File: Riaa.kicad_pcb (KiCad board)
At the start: 2 copper layers, 44 parts, among them J1 power, J2 in, J3 out, U1 TL071, U2 TL072, U3 TL071, U4 TL071

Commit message: layout
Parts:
- moved J2 136.9 mm to (17.8, 143.5)
- moved U4 131.1 mm to (127.0, 94.0), turned to 270 degrees
- moved R17 127.5 mm to (29.2, 123.2)
- moved R18 121.2 mm to (25.4, 132.1)
- moved R28 119.4 mm to (119.4, 121.9)
- moved R20 118.3 mm to (17.8, 125.7)
- moved R23 116.2 mm to (83.8, 128.3)
- moved R25 111.6 mm to (74.9, 120.7)
- moved R27 110.9 mm to (119.4, 108.0)
- moved R22 109.1 mm to (88.9, 116.8)
- moved U3 108.7 mm to (87.6, 95.2), turned to 270 degrees
- moved J3 108.1 mm to (110.5, 129.5)
- moved R24 108.0 mm to (85.1, 111.8)
- moved R15 108.0 mm to (22.9, 110.5)
- moved C9 105.5 mm to (132.1, 116.8)
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
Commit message: layout
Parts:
- moved R28 56.4 mm to (71.1, 92.7), turned to 270 degrees
- moved R23 54.9 mm to (53.3, 82.5), turned to 270 degrees
- moved J2 53.4 mm to (19.1, 90.2), turned to 90 degrees
- moved J1 52.6 mm to (67.3, 36.8)
- moved R27 48.6 mm to (78.7, 81.3), turned to 270 degrees
- moved C9 46.2 mm to (88.9, 100.3), turned to 90 degrees
- moved R22 45.9 mm to (58.4, 82.5), turned to 270 degrees
- moved J3 44.9 mm to (69.8, 110.5), turned to 90 degrees
- moved U4 44.5 mm to (82.5, 94.0)
- moved R16 37.7 mm to (35.6, 83.8), turned to 270 degrees
- moved C4 36.8 mm to (66.0, 48.3), turned to 90 degrees
- moved R24 32.1 mm to (58.4, 94.0), turned to 270 degrees
- moved U3 31.8 mm to (55.9, 94.0)
- moved R17 31.4 mm to (40.6, 94.0), turned to 270 degrees
- moved R18 29.6 mm to (40.6, 106.7), turned to 180 degrees
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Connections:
- R25 pad 1: Net-(R25-Pad1) -> GND
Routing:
- net Net-(C2-Pad1): track 0.00 -> 78.0 mm
- net Net-(C4-Pad1): track 0.00 -> 51.6 mm
- net Net-(J3-Pad1): track 0.00 -> 11.2 mm
- net Net-(R16-Pad2): track 0.00 -> 9.42 mm
- net Net-(C6-Pad1): track 0.00 -> 8.89 mm
- net GND: track 0.00 -> 7.44 mm
- net Net-(C5-Pad1): track 0.00 -> 6.35 mm
- net Net-(C6-Pad2): track 0.00 -> 5.08 mm

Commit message: decoupling
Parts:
- added C10: 100n, Capacitors_THT:C_Rect_L7.2mm_W2.5mm_P5.00mm_FKS2_FKP2_MKS2_MKP2, F.Cu at (67.3, 53.3)
- moved R9 33.2 mm to (77.5, 77.5), turned to 90 degrees
- moved C1 26.2 mm to (52.1, 64.8), turned to 270 degrees
- moved C4 25.5 mm to (68.6, 73.7), turned to 180 degrees
- moved R1 25.4 mm to (64.8, 50.8)
- moved R8 23.3 mm to (72.4, 66.0), turned to 180 degrees
- moved C2 18.2 mm to (58.4, 72.4), turned to 270 degrees
- moved R3 17.6 mm to (54.6, 50.8)
- moved R12 15.3 mm to (74.9, 68.6), turned to 90 degrees
- moved R10 11.4 mm to (85.1, 67.3), turned to 180 degrees
- moved R13 10.9 mm to (85.1, 59.7), turned to 180 degrees
- moved R7 10.9 mm to (62.2, 53.3), turned to 180 degrees
- moved R6 10.5 mm to (54.6, 55.9)
- moved R5 10.5 mm to (62.2, 66.0), turned to 90 degrees
- moved R4 9.92 mm to (59.7, 61.0), turned to 180 degrees
- moved J1 8.98 mm to (68.6, 45.7)
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
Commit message: routing
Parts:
- moved C7 24.3 mm to (49.5, 88.9)
- moved R20 20.4 mm to (43.2, 101.6)
- moved R21 19.1 mm to (45.7, 101.6)
- moved J2 15.9 mm to (33.0, 82.5)
- moved R16 10.8 mm to (43.2, 91.4), turned to 180 degrees
- moved R15 8.03 mm to (40.6, 86.4), turned to 180 degrees
- moved C5 6.84 mm to (35.6, 88.9), turned to 0 degrees
- moved C6 3.81 mm to (33.0, 106.7)
- moved R18 2.54 mm to (40.6, 104.1)
- moved R19 2.54 mm to (40.6, 106.7), turned to 0 degrees
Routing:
- net Net-(C6-Pad1): track 8.89 -> 30.0 mm
- net Net-(C7-Pad1): track 0.00 -> 11.2 mm
- net Net-(J3-Pad1): track 11.2 -> 18.8 mm
- net GND: track 7.44 -> 0.00 mm
- net Net-(C5-Pad1): track 6.35 -> 10.2 mm
- net Net-(C6-Pad2): track 5.08 -> 7.70 mm

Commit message: routing
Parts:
- moved J1 36.9 mm to (67.3, 82.5)
- moved R2 16.6 mm to (54.6, 71.1)
- moved C8 6.48 mm to (58.4, 90.2), turned to 0 degrees
- moved C2 4.02 mm to (59.7, 68.6)
- moved R10 3.81 mm to (85.1, 63.5)
- moved R13 2.84 mm to (82.5, 58.4)
- moved R22 2.84 mm to (55.9, 83.8)
- moved R11 2.54 mm to (77.5, 61.0)
- moved R4 2.54 mm to (59.7, 58.4)
- moved R28 1.80 mm to (69.8, 94.0)
- moved R14 1.27 mm to (74.9, 55.9)
- moved R23 1.27 mm to (53.3, 83.8)
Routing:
- net Net-(C9-Pad1): track 0.00 -> 23.7 mm
- net Net-(C10-Pad1): track 0.00 -> 14.5 mm
- net Net-(C2-Pad1): track 78.0 -> 91.5 mm
- net Net-(C1-Pad1): track 0.00 -> 9.42 mm
- net Net-(R22-Pad2): track 0.00 -> 8.67 mm
- net Net-(R10-Pad2): track 0.00 -> 6.13 mm
- net Net-(R11-Pad1): track 0.00 -> 6.13 mm
- net Net-(R4-Pad1): track 0.00 -> 6.13 mm
- net Net-(R12-Pad2): track 0.00 -> 5.08 mm
- net Net-(C10-Pad2): track 0.00 -> 5.08 mm
- net Net-(R5-Pad2): track 0.00 -> 5.08 mm
- net Net-(C4-Pad1): track 51.6 -> 55.2 mm
- net Net-(R6-Pad1): track 0.00 -> 2.54 mm
- net Net-(R13-Pad1): track 0.00 -> 2.54 mm
- net Net-(R1-Pad1): track 0.00 -> 2.54 mm
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
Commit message: layout
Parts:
- moved C2 24.1 mm to (67.3, 45.7), turned to 0 degrees
- moved C4 21.3 mm to (74.9, 53.3), turned to 0 degrees
- moved C3 16.6 mm to (82.5, 55.9), turned to 90 degrees
- moved R9 11.7 mm to (85.1, 68.6), turned to 180 degrees
- moved C9 7.62 mm to (80.0, 101.6)
- moved J2 6.84 mm to (30.5, 88.9)
- moved U4 6.35 mm to (76.2, 94.0)
- moved R2 5.68 mm to (59.7, 68.6)
- moved R28 3.81 mm to (66.0, 94.0)
- moved R13 3.59 mm to (85.1, 61.0)
- moved C8 2.84 mm to (61.0, 91.4), turned to 90 degrees
- moved R10 2.54 mm to (85.1, 66.0)
- moved R25 2.54 mm to (63.5, 94.0)
- moved C1 2.54 mm to (52.1, 62.2)
- moved C5 2.54 mm to (38.1, 88.9)
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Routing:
- net GND: track 0.00 -> 34.1 mm
- net Net-(R22-Pad2): track 8.67 -> 24.2 mm
- net Net-(C2-Pad1): track 91.5 -> 76.0 mm
- net Net-(R1-Pad1): track 2.54 -> 17.3 mm
- net Net-(C3-Pad1): track 2.54 -> 14.8 mm
- net Net-(C4-Pad1): track 55.2 -> 46.5 mm
- net Net-(C9-Pad1): track 23.7 -> 30.8 mm
- net Net-(C5-Pad1): track 10.2 -> 15.2 mm
- net Net-(J3-Pad1): track 18.8 -> 16.3 mm
- net Net-(C8-Pad1): track 0.00 -> 2.54 mm
- net Net-(C7-Pad1): track 11.2 -> 13.8 mm
- net Net-(R10-Pad2): track 6.13 -> 5.08 mm
- net Net-(R13-Pad1): track 2.54 -> 3.59 mm
- net Net-(R11-Pad1): track 6.13 -> 5.08 mm

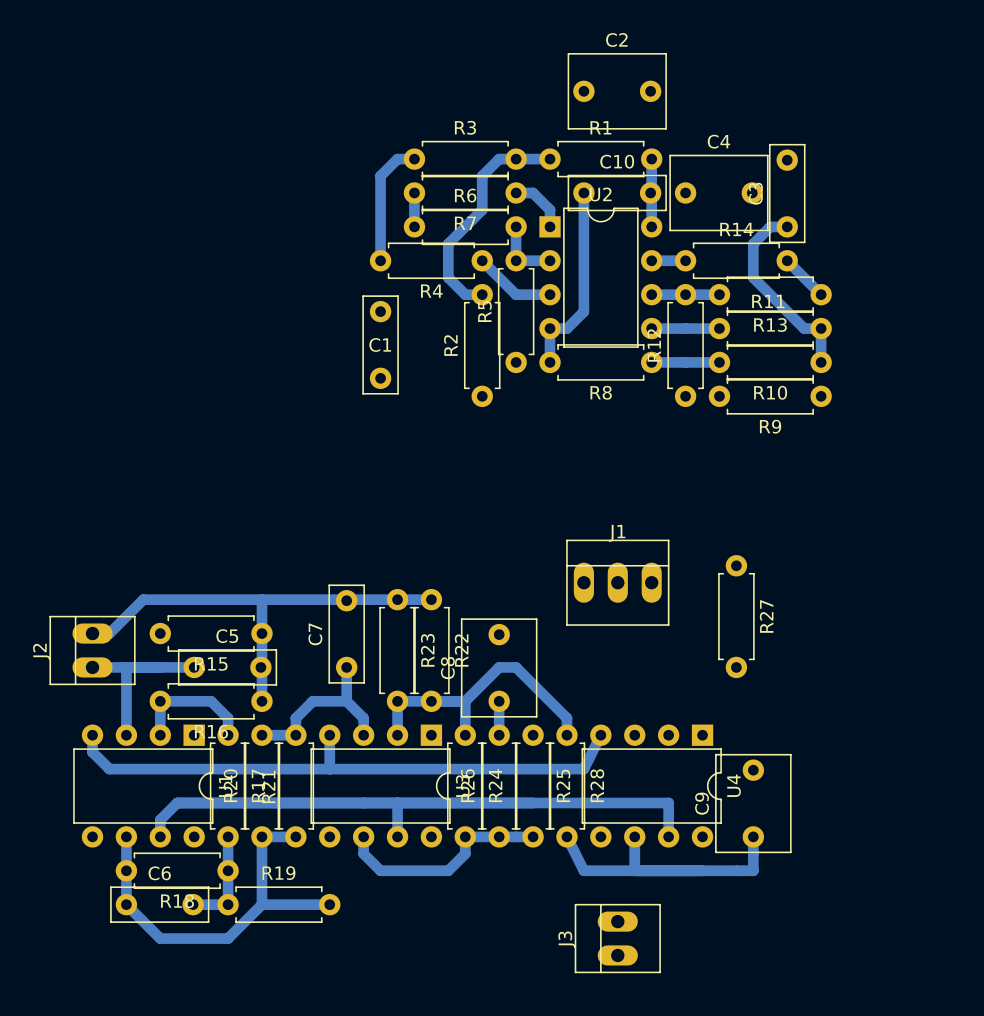
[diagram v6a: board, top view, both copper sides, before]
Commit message: 65x30mm
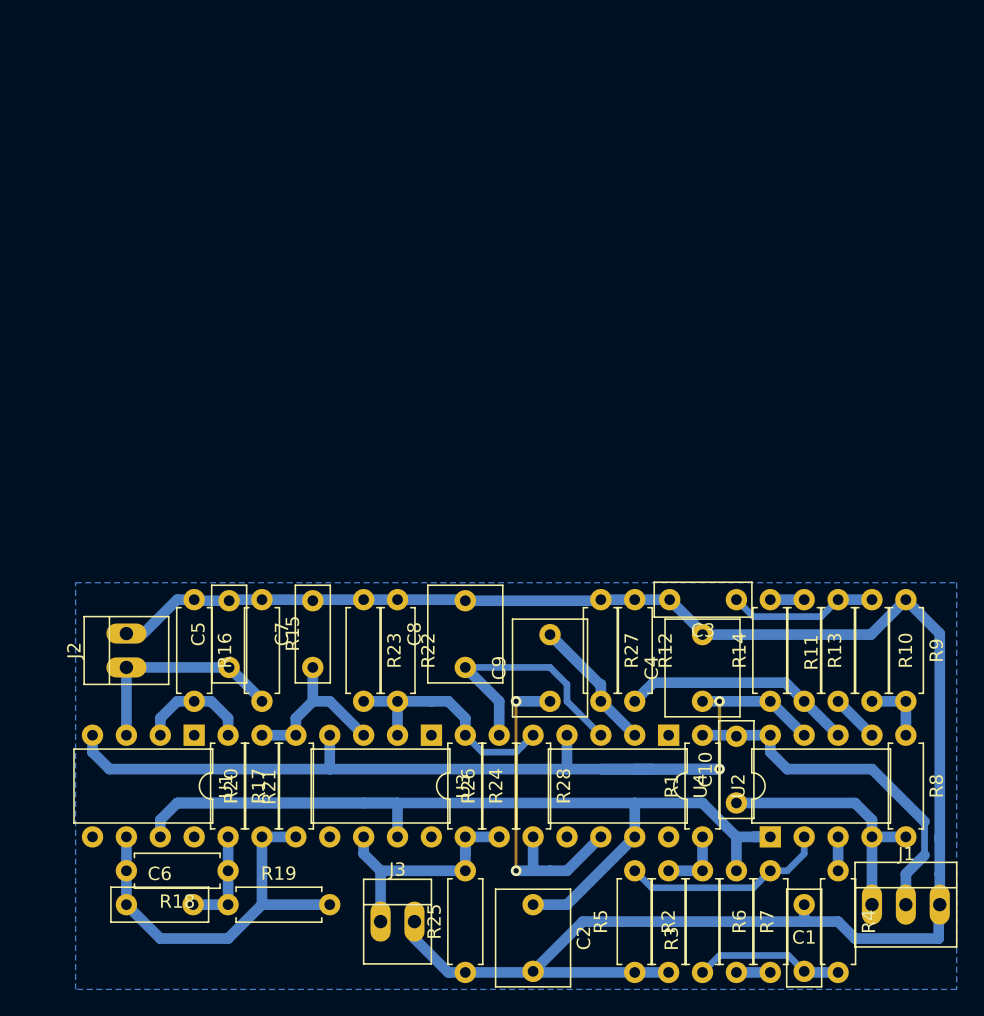
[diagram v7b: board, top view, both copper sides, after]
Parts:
- moved R3 64.7 mm to (76.2, 111.8), turned to 90 degrees
- moved R6 61.9 mm to (81.3, 111.8), turned to 90 degrees
- moved C2 61.1 mm to (63.5, 106.7), turned to 270 degrees
- moved C1 58.8 mm to (83.8, 111.7), turned to 90 degrees
- moved R7 53.4 mm to (78.7, 104.1), turned to 270 degrees
- moved R4 52.9 mm to (86.4, 104.1), turned to 270 degrees
- moved R1 52.1 mm to (76.2, 101.6), turned to 90 degrees
- moved U2 48.6 mm to (81.3, 101.6), turned to 90 degrees
- moved C10 47.1 mm to (78.7, 99.1), turned to 90 degrees
- moved R5 46.6 mm to (71.1, 111.8)
- moved R2 45.4 mm to (73.7, 111.8)
- moved C4 38.1 mm to (76.2, 91.4), turned to 90 degrees
- moved R8 33.8 mm to (91.4, 94.0), turned to 270 degrees
- moved R14 33.6 mm to (81.3, 91.4), turned to 90 degrees
- moved J1 32.4 mm to (88.9, 106.7)
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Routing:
- net GND: track 34.1 -> 143.8 mm
- net Net-(C4-Pad1): track 46.5 -> 79.0 mm, vias 0 -> 2
- net Net-(C10-Pad2): track 5.08 -> 28.1 mm
- net Net-(C8-Pad1): track 2.54 -> 19.1 mm
- net Net-(R12-Pad2): track 5.08 -> 17.5 mm
- net Net-(R1-Pad1): track 17.3 -> 5.08 mm
- net Net-(R5-Pad2): track 5.08 -> 15.5 mm
- net Net-(C9-Pad2): track 0.00 -> 10.2 mm
- net Net-(C2-Pad1): track 76.0 -> 83.7 mm
- net Net-(R22-Pad2): track 24.2 -> 18.1 mm
- net Net-(C9-Pad1): track 30.8 -> 25.2 mm, vias 0 -> 2
- net Net-(C10-Pad1): track 14.5 -> 19.6 mm
- net Net-(R4-Pad1): track 6.13 -> 2.54 mm
- net Net-(C3-Pad1): track 14.8 -> 11.2 mm
- net Net-(J3-Pad1): track 16.3 -> 19.6 mm
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- added copper zone on B.Cu, net GND
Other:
- net class Default: clearance 0.2 -> 0
- rule trace_clearance: 0.2 -> 0
